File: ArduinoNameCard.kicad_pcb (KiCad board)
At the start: 2 copper layers, 91 x 55 mm, 30 parts, among them J1 USB_B_Micro, J2 Conn_01x04, J3 Conn_01x06, J4 Conn_01x08, J5 Conn_01x06, SW1 SW_Push

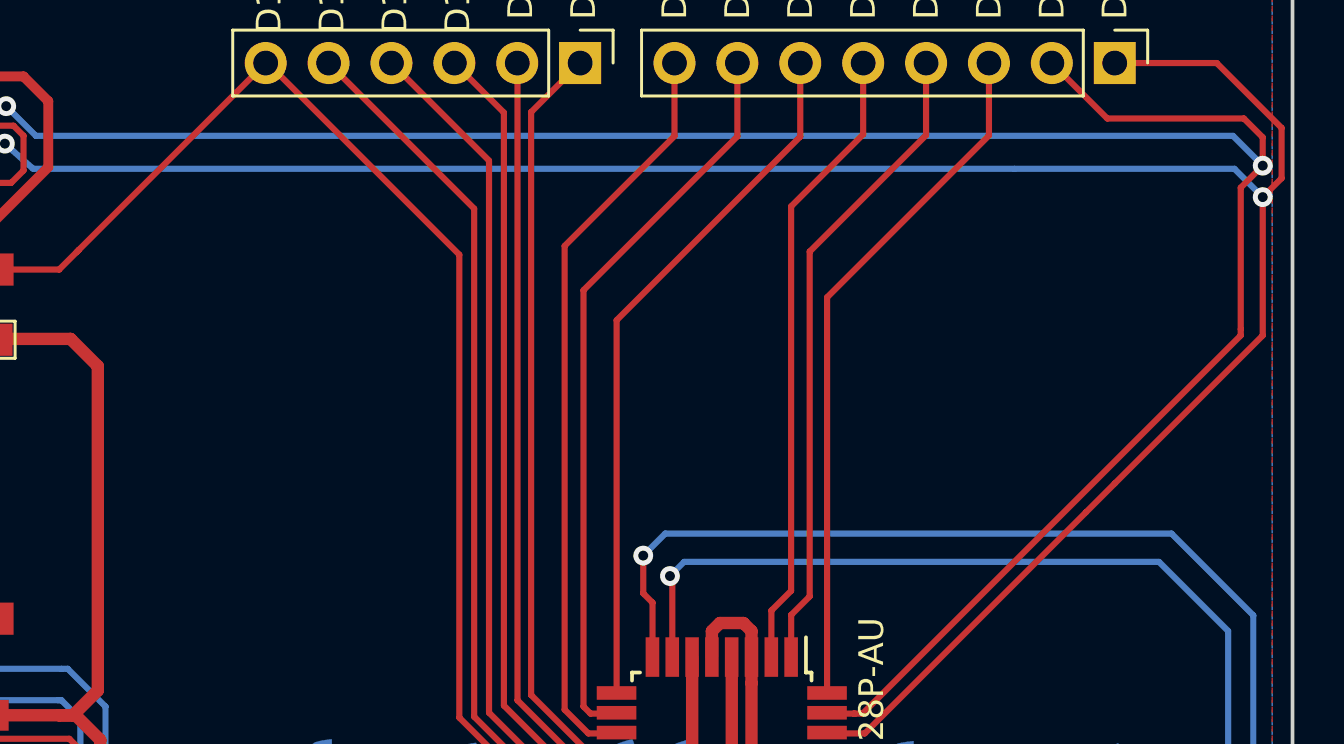
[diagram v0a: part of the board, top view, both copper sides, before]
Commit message: とりあえず、実動したら、twoBoardブランチにも実装する
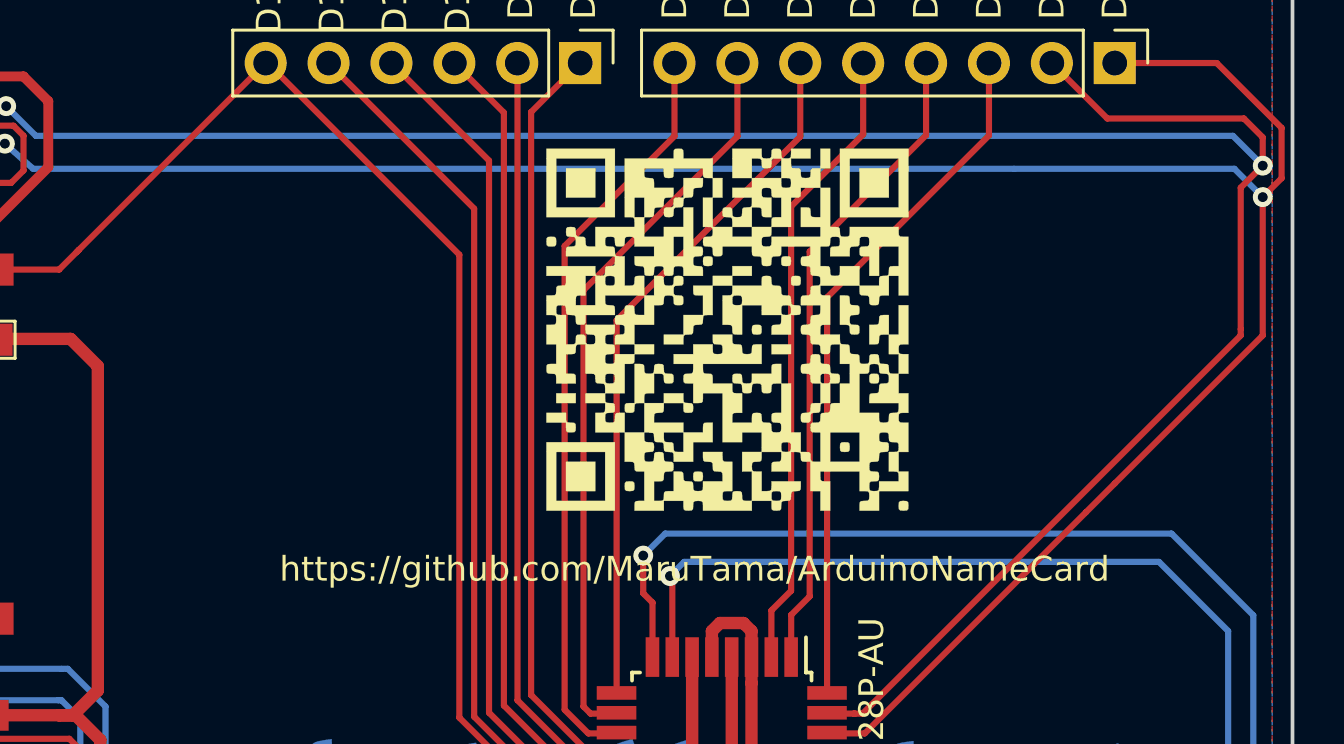
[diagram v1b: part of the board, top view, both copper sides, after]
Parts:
- G***: moved to F.Cu
- moved G*** 55.2 mm to (163.9, 76.7)
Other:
- board text added: "Free space"
- board text added: "https://github.com/MaruTama/ArduinoNameCard"
- board text removed: "github"

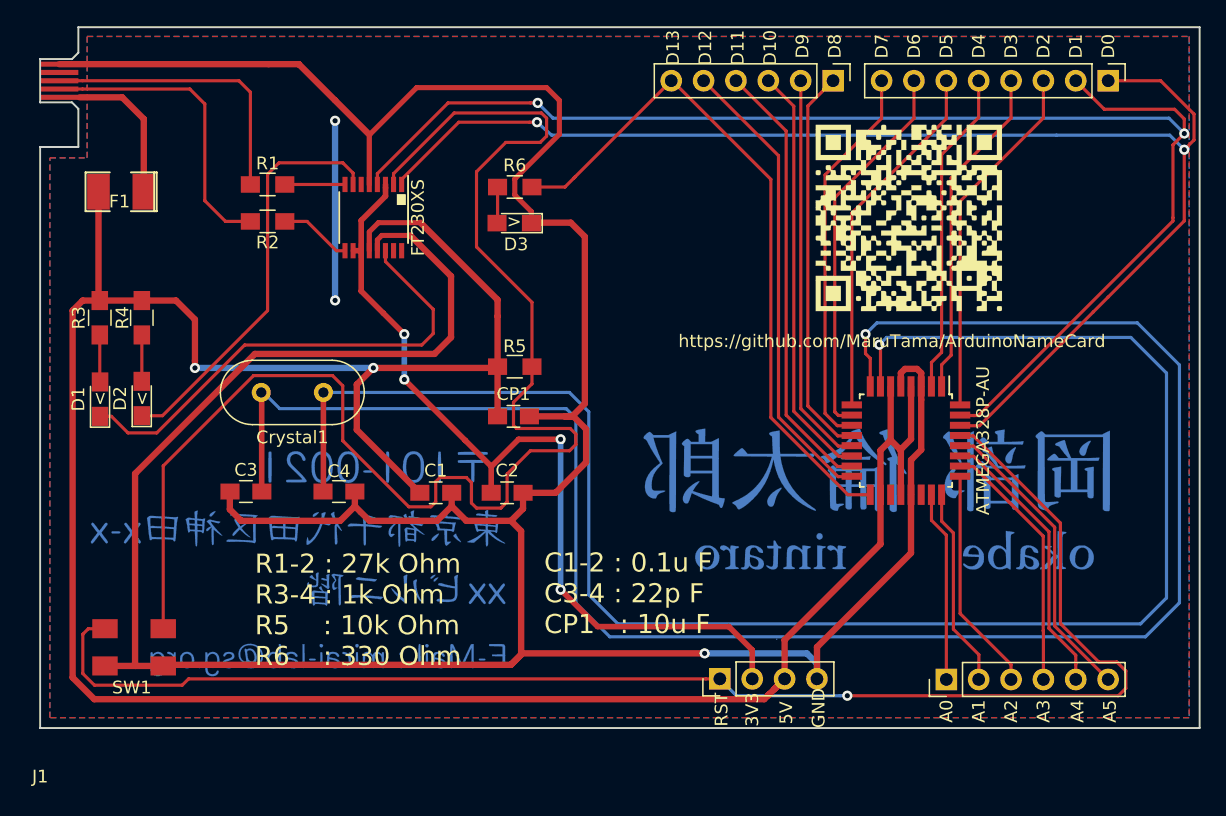
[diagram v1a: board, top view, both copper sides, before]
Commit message: FT231Xに変更した。
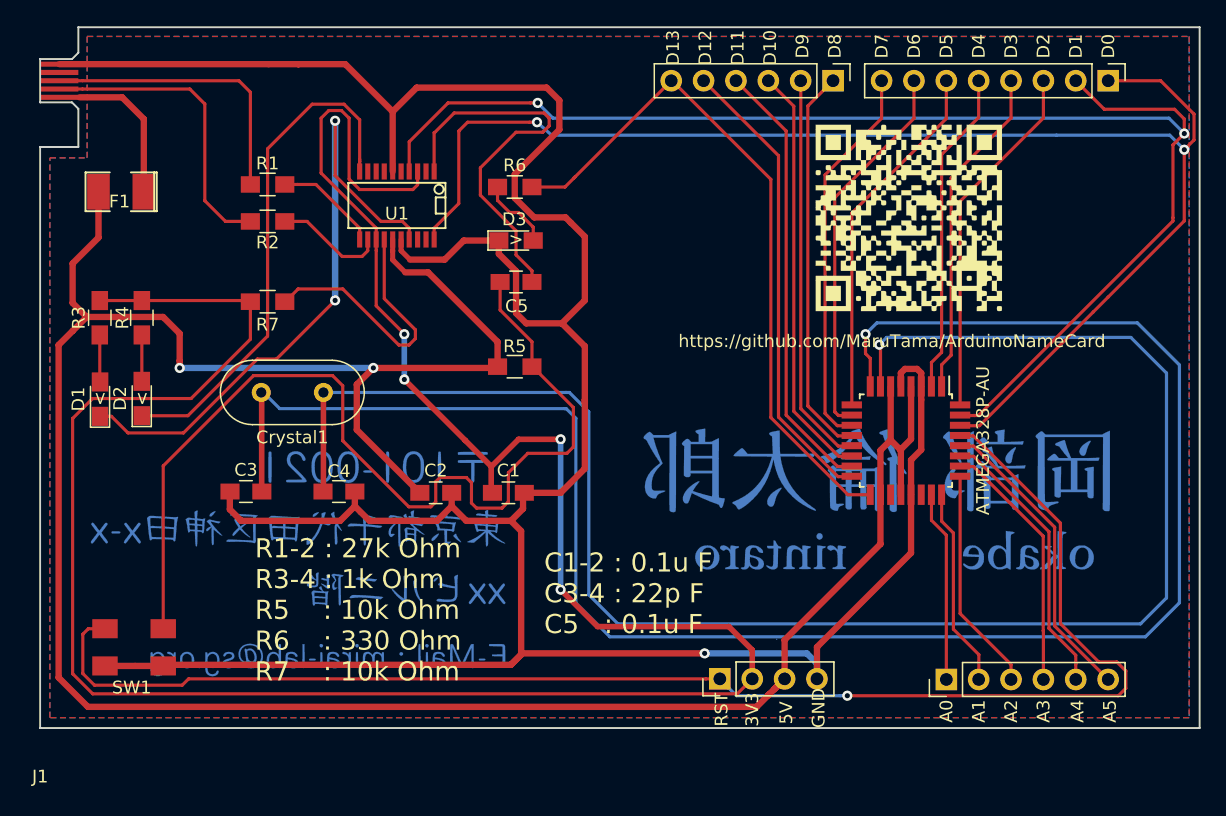
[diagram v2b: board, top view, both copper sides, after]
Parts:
- removed CP1: 10u, Capacitors_SMD:C_0805_HandSoldering
- removed FT230XS: FT230XS, Housings_SSOP:SSOP-16_3.9x4.9mm_Pitch0.635mm
- added C5: 0.1u, Capacitors_SMD:C_0805_HandSoldering, F.Cu at (133.1, 81.8)
- added R7: 10k, Resistors_SMD:R_0805_HandSoldering, F.Cu at (113.6, 83.3)
- added U1: FT231XS, SMD_Packages:SSOP-20, F.Cu at (123.8, 75.8)
- D1: value RED -> RED(TX)
- D2: value GREEN -> GREEN(RX)
- moved C1 5.70 mm to (132.5, 98.3)
- moved C2 5.60 mm to (126.8, 98.3)
- moved D3 1.37 mm to (133.1, 78.5), turned to 0 degrees
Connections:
- net RTS renamed DTR
- C1 pad 1: 5V -> 3V3
- C2 pad 1: 3V3 -> 5V
- R3 pad 1: 5V -> 3V3
- R4 pad 1: 5V -> 3V3
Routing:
- net 3V3: track 67.4 -> 193.4 mm
- net GND: track 280.5 -> 238.9 mm
- net DTR: track 228.3 -> 192.1 mm
- net Net-(C5-Pad2): track 0.00 -> 31.1 mm
- net Net-(R7-Pad2): track 0.00 -> 21.6 mm
- net (no net): track 14.1 -> 0.00 mm, vias 2 -> 0
- net Net-(D1-Pad1): track 38.0 -> 50.1 mm, vias 0 -> 2
- net Net-(D2-Pad1): track 32.4 -> 40.7 mm
- net 5V: track 206.5 -> 199.4 mm
- net D+: track 4.73 -> 8.19 mm
- net D-: track 5.68 -> 8.72 mm
- net Net-(D3-Pad2): track 2.85 -> 5.77 mm
- net TX: track 105.3 -> 108.2 mm
- net RX: track 108.7 -> 106.6 mm
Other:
- board text added: "C1-2 : 0.1u F C3-4 : 22p F C5 : 0.1u F"
- board text added: "R1-2 : 27k Ohm R3-4 : 1k Ohm R5 : 10k Ohm R6 : 330 Ohm R7 : 10k Ohm"
- board text removed: "."
- board text removed: "C1-2 : 0.1u F C3-4 : 22p F CP1 : 10u F"
- board text removed: "R1-2 : 27k Ohm R3-4 : 1k Ohm R5 : 10k Ohm R6 : 330 Ohm"

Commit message: 部品の並びなどを修正した。
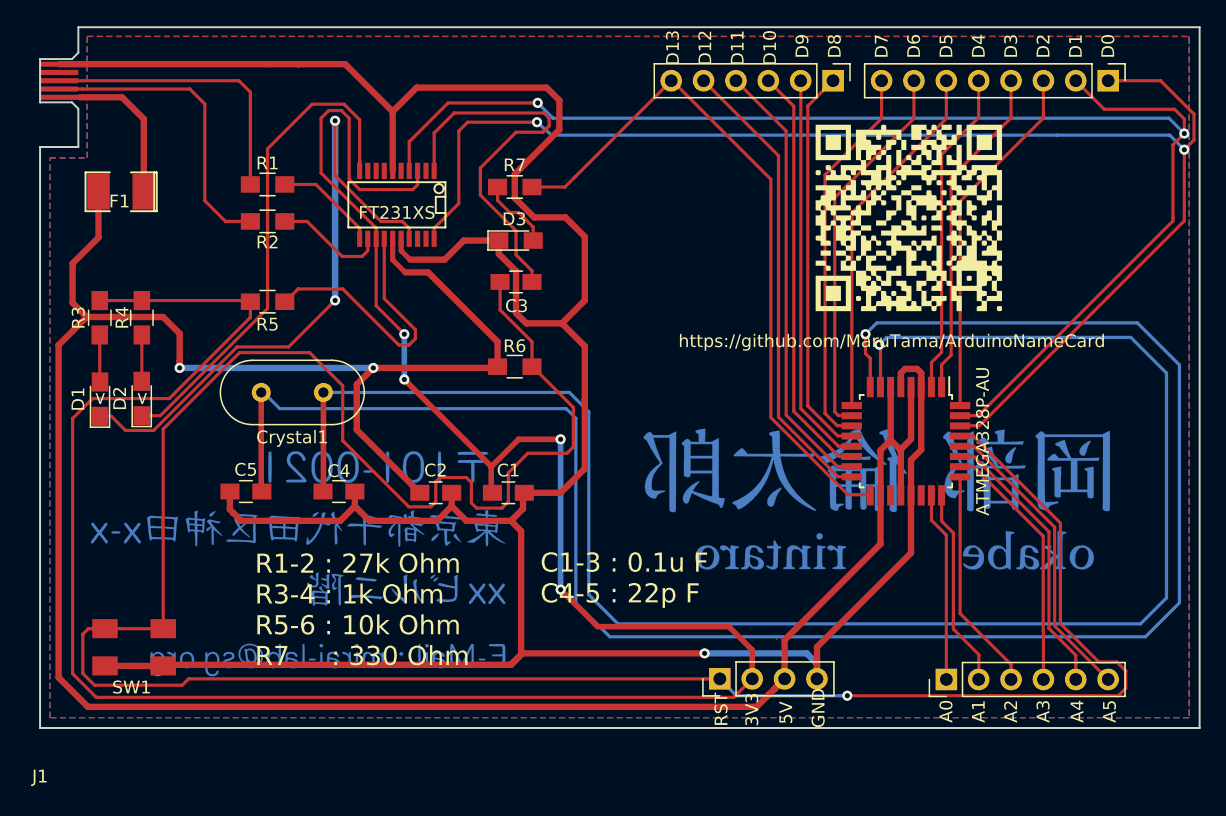
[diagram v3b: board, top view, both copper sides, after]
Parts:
- removed U1: FT231XS, SMD_Packages:SSOP-20
- added FT231XS: FT231XS, SMD_Packages:SSOP-20, F.Cu at (123.8, 75.7)
- renumbered C5 to C3, C3 to C5, R7 to R5, R5 to R6, R6 to R7
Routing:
- net DTR: track 192.1 -> 199.8 mm
- net Net-(D2-Pad1): track 40.7 -> 39.4 mm
- net 3V3: track 193.4 -> 192.6 mm
- net Net-(C5-Pad1): track 146.8 -> 147.3 mm
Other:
- board text added: "C1-3 : 0.1u F C4-5 : 22p F"
- board text added: "R1-2 : 27k Ohm R3-4 : 1k Ohm R5-6 : 10k Ohm R7 : 330 Ohm"
- board text removed: "C1-2 : 0.1u F C3-4 : 22p F C5 : 0.1u F"
- board text removed: "R1-2 : 27k Ohm R3-4 : 1k Ohm R5 : 10k Ohm R6 : 330 Ohm R7 : 10k Ohm"
